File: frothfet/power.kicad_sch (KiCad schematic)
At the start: 46 parts, among them J2 Screw_Terminal_01x08, J3 Screw_Terminal_01x08, U26 TPS7A2033PDBVR, U27 XL1509-5.0, U28 MCP3425A0T-ECH, U29 MAX40200AUK

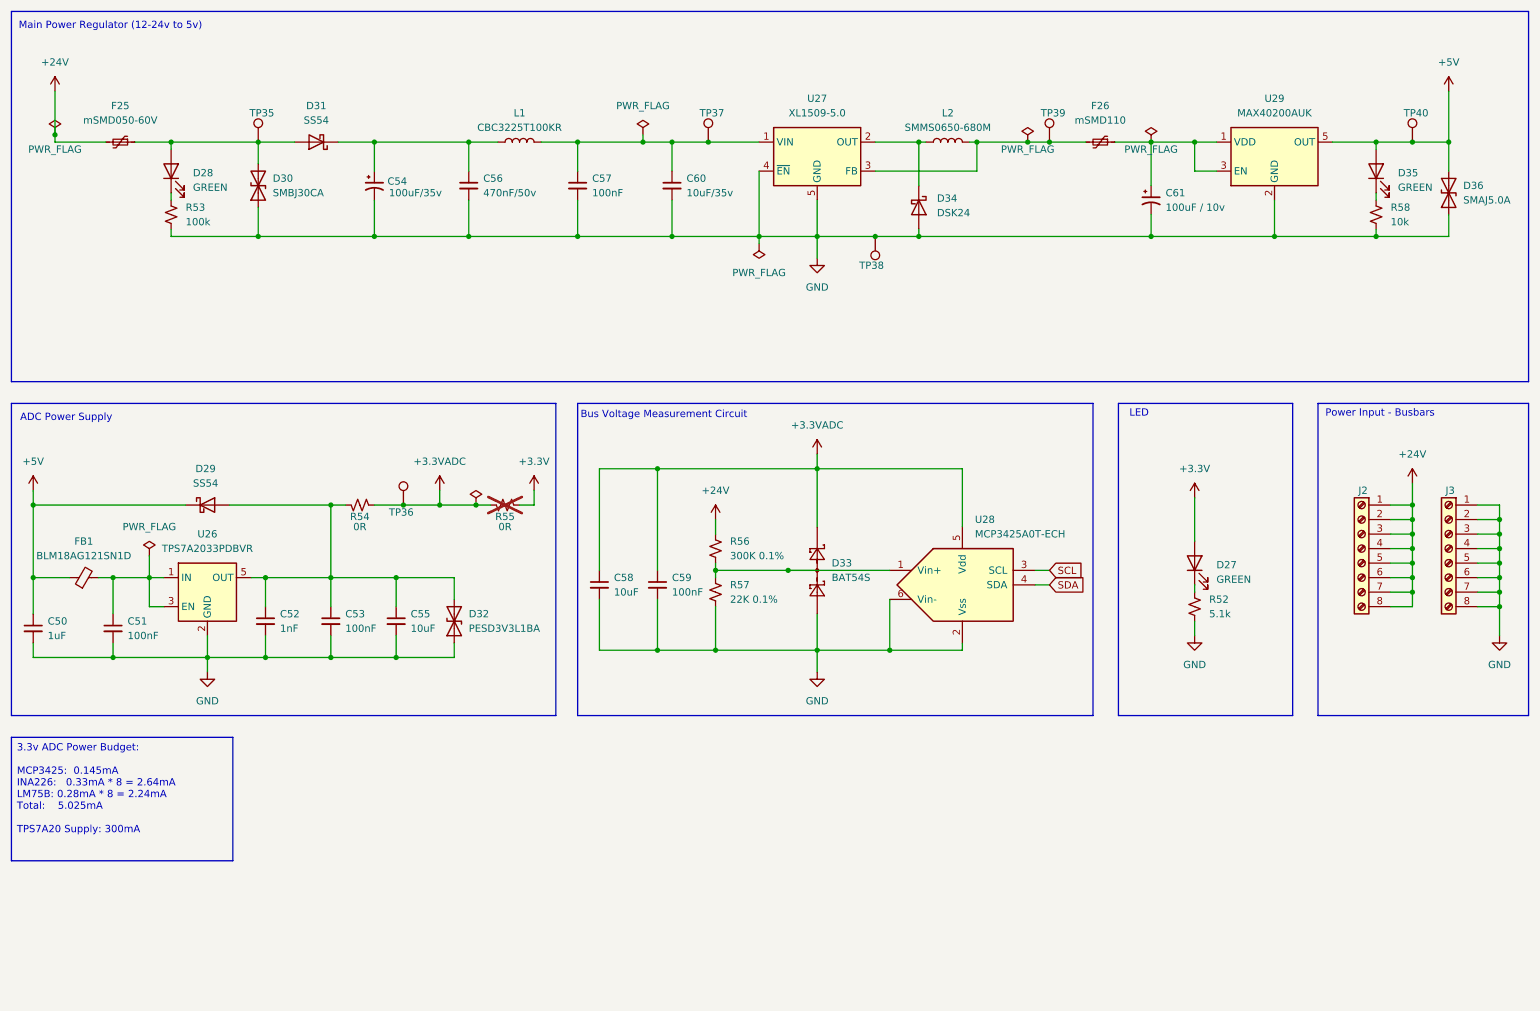
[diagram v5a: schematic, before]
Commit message: add esd protection to each channel output
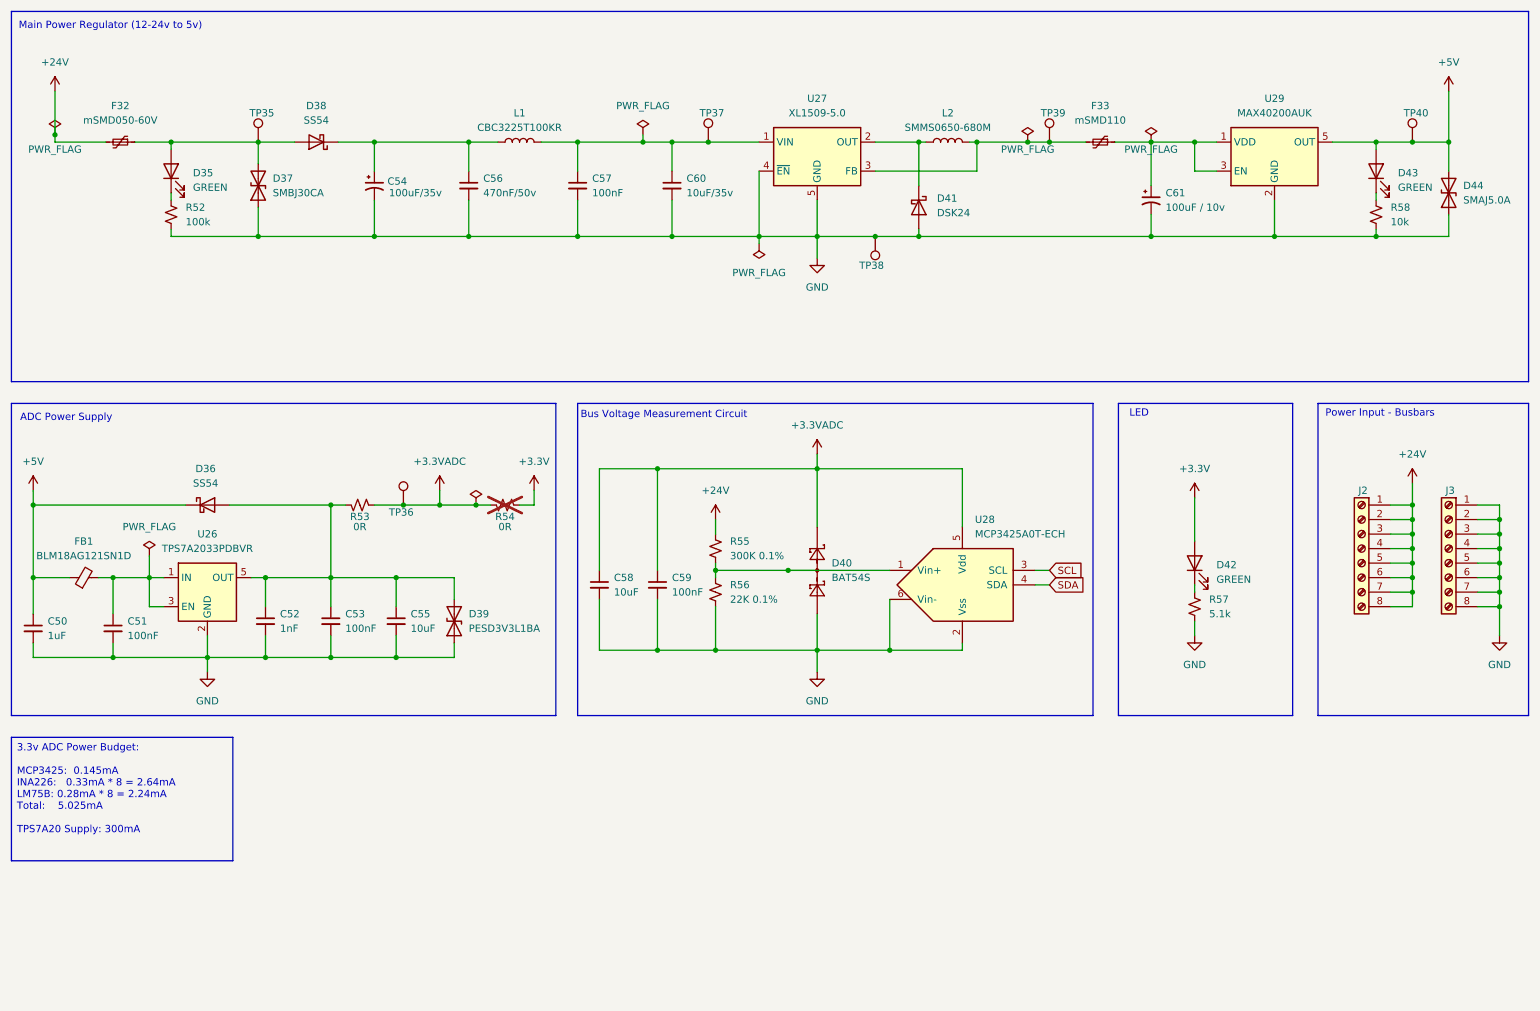
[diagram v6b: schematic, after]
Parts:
- renumbered D28 to D35, D29 to D36, D30 to D37, D31 to D38, D32 to D39, D33 to D40, D34 to D41, D27 to D42, D35 to D43, D36 to D44, F25 to F32, F26 to F33, R53 to R52, R54 to R53, R55 to R54, R56 to R55, R57 to R56, R52 to R57
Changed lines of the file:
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@@
 		(dnp no)
 		(fields_autoplaced yes)
-		(property "Reference" "D33"
+		(property "Reference" "D40"
 			(at 158.75 111.76 90)
 			(effects
@@
 			(project "8ch-mosfet"
 				(path "/c83c6236-96e9-46ad-9d7a-9e2efa4a7966/e112a34f-fd2f-43cb-bf5d-a7f5e57b6bef"
-					(reference "D33")
+					(reference "D40")
 					(unit 1)
 				)
@@
 		(dnp no)
 		(fields_autoplaced yes)
-		(property "Reference" "R53"
+		(property "Reference" "R52"
 			(at 45.72 49.5299 0)
 			(effects
@@
 			(project "frothfet"
 				(path "/c83c6236-96e9-46ad-9d7a-9e2efa4a7966/e112a34f-fd2f-43cb-bf5d-a7f5e57b6bef"
-					(reference "R53")
+					(reference "R52")
 					(unit 1)
 				)
@@
 		(dnp no)
 		(fields_autoplaced yes)
-		(property "Reference" "D34"
+		(property "Reference" "D41"
 			(at 177.165 47.9425 90)
 			(effects
@@
 			(project "8ch-mosfet"
 				(path "/c83c6236-96e9-46ad-9d7a-9e2efa4a7966/e112a34f-fd2f-43cb-bf5d-a7f5e57b6bef"
-					(reference "D34")
+					(reference "D41")
 					(unit 1)
 				)
@@
 		(dnp no)
 		(fields_autoplaced yes)
-		(property "Reference" "D28"
+		(property "Reference" "D35"
 			(at 46.99 43.4974 90)
 			(effects
@@
 			(project "frothfet"
 				(path "/c83c6236-96e9-46ad-9d7a-9e2efa4a7966/e112a34f-fd2f-43cb-bf5d-a7f5e57b6bef"
-					(reference "D28")
+					(reference "D35")
 					(unit 1)
 				)
@@
 		(dnp no)
 		(fields_autoplaced yes)
-		(property "Reference" "#PWR0137"
+		(property "Reference" "#PWR0135"
 			(at 106.68 102.87 0)
 			(effects
@@
 			(project "frothfet"
 				(path "/c83c6236-96e9-46ad-9d7a-9e2efa4a7966/e112a34f-fd2f-43cb-bf5d-a7f5e57b6bef"
-					(reference "#PWR0137")
+					(reference "#PWR0135")
 					(unit 1)
 				)
@@
 		(dnp no)
 		(fields_autoplaced yes)
-		(property "Reference" "#PWR0133"
+		(property "Reference" "#PWR0140"
 			(at 222.25 104.14 0)
 			(effects
@@
 			(project "frothfet"
 				(path "/c83c6236-96e9-46ad-9d7a-9e2efa4a7966/e112a34f-fd2f-43cb-bf5d-a7f5e57b6bef"
-					(reference "#PWR0133")
+					(reference "#PWR0140")
 					(unit 1)
 				)
@@
 		(dnp no)
 		(fields_autoplaced yes)
-		(property "Reference" "D27"
+		(property "Reference" "D42"
 			(at 226.06 112.0774 90)
 			(effects
@@
 			(project "frothfet"
 				(path "/c83c6236-96e9-46ad-9d7a-9e2efa4a7966/e112a34f-fd2f-43cb-bf5d-a7f5e57b6bef"
-					(reference "D27")
+					(reference "D42")
 					(unit 1)
 				)
@@
 		(dnp no)
 		(fields_autoplaced yes)
-		(property "Reference" "#PWR0141"
+		(property "Reference" "#PWR0139"
 			(at 156.21 137.16 0)
 			(effects
@@
 			(project "frothfet"
 				(path "/c83c6236-96e9-46ad-9d7a-9e2efa4a7966/e112a34f-fd2f-43cb-bf5d-a7f5e57b6bef"
-					(reference "#PWR0141")
+					(reference "#PWR0139")
 					(unit 1)
 				)
@@
 		(dnp no)
 		(fields_autoplaced yes)
-		(property "Reference" "#PWR0136"
+		(property "Reference" "#PWR0134"
 			(at 86.36 100.33 0)
 			(effects
@@
 			(project ""
 				(path "/c83c6236-96e9-46ad-9d7a-9e2efa4a7966/e112a34f-fd2f-43cb-bf5d-a7f5e57b6bef"
-					(reference "#PWR0136")
+					(reference "#PWR0134")
 					(unit 1)
 				)
@@
 		(on_board yes)
 		(dnp no)
-		(property "Reference" "D30"
+		(property "Reference" "D37"
 			(at 60.96 44.45 90)
 			(effects
@@
 			(project "8ch-mosfet"
 				(path "/c83c6236-96e9-46ad-9d7a-9e2efa4a7966/e112a34f-fd2f-43cb-bf5d-a7f5e57b6bef"
-					(reference "D30")
+					(reference "D37")
 					(unit 1)
 				)
@@
 		(on_board yes)
 		(dnp no)
-		(property "Reference" "D29"
+		(property "Reference" "D36"
 			(at 49.2125 95.25 0)
 			(effects
@@
 			(project "frothfet"
 				(path "/c83c6236-96e9-46ad-9d7a-9e2efa4a7966/e112a34f-fd2f-43cb-bf5d-a7f5e57b6bef"
-					(reference "D29")
+					(reference "D36")
 					(unit 1)
 				)
@@
 		(dnp no)
 		(fields_autoplaced yes)
-		(property "Reference" "R56"
+		(property "Reference" "R55"
 			(at 140.97 107.95 0)
 			(effects
@@
 			(project "8ch-mosfet"
 				(path "/c83c6236-96e9-46ad-9d7a-9e2efa4a7966/e112a34f-fd2f-43cb-bf5d-a7f5e57b6bef"
-					(reference "R56")
+					(reference "R55")
 					(unit 1)
 				)
@@
 		(dnp no)
 		(fields_autoplaced yes)
-		(property "Reference" "#PWR0134"
+		(property "Reference" "#PWR0141"
 			(at 222.25 130.81 0)
 			(effects
@@
 			(project "frothfet"
 				(path "/c83c6236-96e9-46ad-9d7a-9e2efa4a7966/e112a34f-fd2f-43cb-bf5d-a7f5e57b6bef"
-					(reference "#PWR0134")
+					(reference "#PWR0141")
 					(unit 1)
 				)
@@
 		(dnp no)
 		(fields_autoplaced yes)
-		(property "Reference" "#PWR0138"
+		(property "Reference" "#PWR0136"
 			(at 138.43 107.95 0)
 			(effects
@@
 			(project "8ch-mosfet"
 				(path "/c83c6236-96e9-46ad-9d7a-9e2efa4a7966/e112a34f-fd2f-43cb-bf5d-a7f5e57b6bef"
-					(reference "#PWR0138")
+					(reference "#PWR0136")
 					(unit 1)
 				)
@@
 		(dnp no)
 		(fields_autoplaced yes)
-		(property "Reference" "F26"
+		(property "Reference" "F33"
 			(at 205.74 31.75 90)
 			(effects
@@
 			(project "8ch-mosfet"
 				(path "/c83c6236-96e9-46ad-9d7a-9e2efa4a7966/e112a34f-fd2f-43cb-bf5d-a7f5e57b6bef"
-					(reference "F26")
+					(reference "F33")
 					(unit 1)
 				)
@@
 		(dnp no)
 		(fields_autoplaced yes)
-		(property "Reference" "D35"
+		(property "Reference" "D43"
 			(at 257.81 43.4974 90)
 			(effects
@@
 			(project "frothfet"
 				(path "/c83c6236-96e9-46ad-9d7a-9e2efa4a7966/e112a34f-fd2f-43cb-bf5d-a7f5e57b6bef"
-					(reference "D35")
+					(reference "D43")
 					(unit 1)
 				)
@@
 		(dnp no)
 		(fields_autoplaced yes)
-		(property "Reference" "F25"
+		(property "Reference" "F32"
 			(at 34.29 31.75 90)
 			(effects
@@
 			(project "8ch-mosfet"
 				(path "/c83c6236-96e9-46ad-9d7a-9e2efa4a7966/e112a34f-fd2f-43cb-bf5d-a7f5e57b6bef"
-					(reference "F25")
+					(reference "F32")
 					(unit 1)
 				)
@@
 		(dnp no)
 		(fields_autoplaced yes)
-		(property "Reference" "#PWR0139"
+		(property "Reference" "#PWR0137"
 			(at 156.21 64.77 0)
 			(effects
@@
 			(project "8ch-mosfet"
 				(path "/c83c6236-96e9-46ad-9d7a-9e2efa4a7966/e112a34f-fd2f-43cb-bf5d-a7f5e57b6bef"
-					(reference "#PWR0139")
+					(reference "#PWR0137")
 					(unit 1)
 				)
@@
 		(on_board yes)
 		(dnp no)
-		(property "Reference" "R54"
+		(property "Reference" "R53"
 			(at 76.2 103.632 90)
 			(effects
@@
 			(project "frothfet"
 				(path "/c83c6236-96e9-46ad-9d7a-9e2efa4a7966/e112a34f-fd2f-43cb-bf5d-a7f5e57b6bef"
-					(reference "R54")
+					(reference "R53")
 					(unit 1)
 				)
@@
 		(on_board yes)
 		(dnp no)
-		(property "Reference" "D36"
+		(property "Reference" "D44"
 			(at 269.24 45.72 90)
 			(effects
@@
 			(project "frothfet"
 				(path "/c83c6236-96e9-46ad-9d7a-9e2efa4a7966/e112a34f-fd2f-43cb-bf5d-a7f5e57b6bef"
-					(reference "D36")
+					(reference "D44")
 					(unit 1)
 				)
@@
 		(dnp no)
 		(fields_autoplaced yes)
-		(property "Reference" "#PWR0135"
+		(property "Reference" "#PWR0133"
 			(at 49.53 137.16 0)
 			(effects
@@
 			(project ""
 				(path "/c83c6236-96e9-46ad-9d7a-9e2efa4a7966/e112a34f-fd2f-43cb-bf5d-a7f5e57b6bef"
-					(reference "#PWR0135")
+					(reference "#PWR0133")
 					(unit 1)
 				)
@@
 		(on_board yes)
 		(dnp yes)
-		(property "Reference" "R55"
+		(property "Reference" "R54"
 			(at 101.6 103.632 90)
 			(effects
@@
 			(project "frothfet"
 				(path "/c83c6236-96e9-46ad-9d7a-9e2efa4a7966/e112a34f-fd2f-43cb-bf5d-a7f5e57b6bef"
-					(reference "R55")
+					(reference "R54")
 					(unit 1)
 				)
@@
 		(dnp no)
 		(fields_autoplaced yes)
-		(property "Reference" "R57"
+		(property "Reference" "R56"
 			(at 140.97 115.57 0)
 			(effects
@@
 			(project "8ch-mosfet"
 				(path "/c83c6236-96e9-46ad-9d7a-9e2efa4a7966/e112a34f-fd2f-43cb-bf5d-a7f5e57b6bef"
-					(reference "R57")
+					(reference "R56")
 					(unit 1)
 				)
@@
 		(dnp no)
 		(fields_autoplaced yes)
-		(property "Reference" "D31"
+		(property "Reference" "D38"
 			(at 68.58 31.75 0)
 			(effects
@@
 			(project "8ch-mosfet"
 				(path "/c83c6236-96e9-46ad-9d7a-9e2efa4a7966/e112a34f-fd2f-43cb-bf5d-a7f5e57b6bef"
-					(reference "D31")
+					(reference "D38")
 					(unit 1)
 				)
@@
 		(on_board yes)
 		(dnp no)
-		(property "Reference" "D32"
+		(property "Reference" "D39"
 			(at 95.25 120.65 90)
 			(effects
@@
 			(project "frothfet"
 				(path "/c83c6236-96e9-46ad-9d7a-9e2efa4a7966/e112a34f-fd2f-43cb-bf5d-a7f5e57b6bef"
-					(reference "D32")
+					(reference "D39")
 					(unit 1)
 				)
@@
 		(dnp no)
 		(fields_autoplaced yes)
-		(property "Reference" "R52"
+		(property "Reference" "R57"
 			(at 224.79 118.1099 0)
 			(effects
@@
 			(project "frothfet"
 				(path "/c83c6236-96e9-46ad-9d7a-9e2efa4a7966/e112a34f-fd2f-43cb-bf5d-a7f5e57b6bef"
-					(reference "R52")
+					(reference "R57")
 					(unit 1)
 				)
@@
 		(dnp no)
 		(fields_autoplaced yes)
-		(property "Reference" "#PWR0140"
+		(property "Reference" "#PWR0138"
 			(at 160.02 93.98 0)
 			(effects
@@
 			(project "frothfet"
 				(path "/c83c6236-96e9-46ad-9d7a-9e2efa4a7966/e112a34f-fd2f-43cb-bf5d-a7f5e57b6bef"
-					(reference "#PWR0140")
+					(reference "#PWR0138")
 					(unit 1)
 				)

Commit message: pulled in latest version of esp32 schematic
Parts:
- removed D42: GREEN, LED_SMD:LED_0603_1608Metric, symbol Device:LED
- removed R57: 5.1k, Resistor_SMD:R_0603_1608Metric, symbol Device:R_Small_US
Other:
- note removed: "LED"

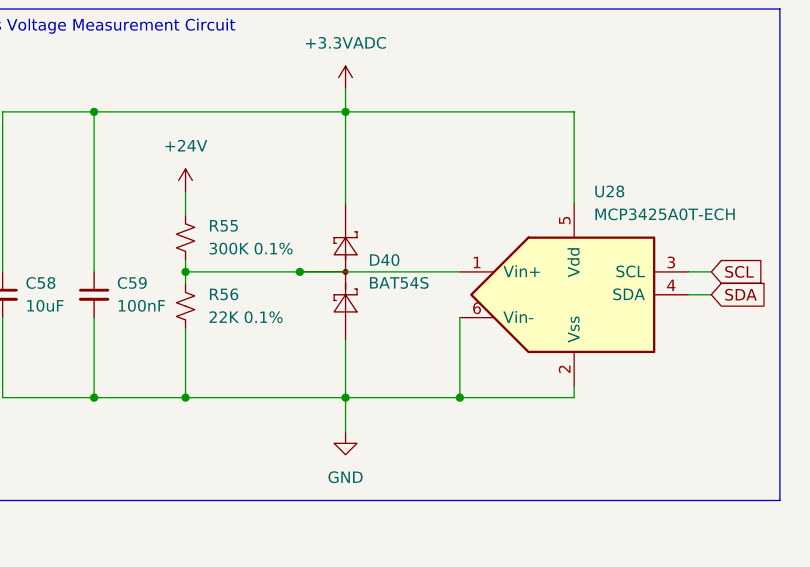
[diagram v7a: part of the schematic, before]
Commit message: switched to bav199 on bus voltage
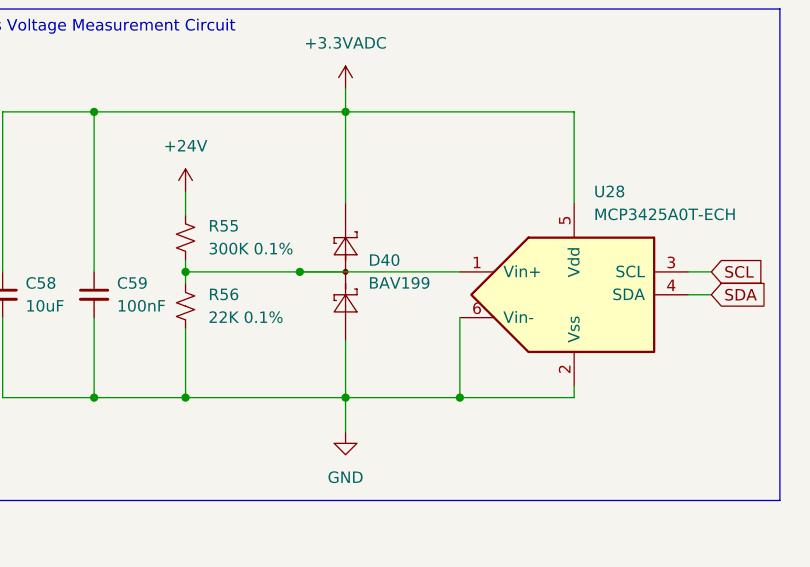
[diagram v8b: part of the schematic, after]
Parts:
- D40: value BAT54S -> BAV199; LCSC C727126 -> C40919
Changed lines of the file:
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@@
 			)
 		)
-		(property "Value" "BAT54S"
+		(property "Value" "BAV199"
 			(at 158.75 114.3 90)
 			(effects
@@
 			)
 		)
-		(property "Datasheet" "https://www.diodes.com/assets/Datasheets/ds11005.pdf"
+		(property "Datasheet" "https://www.lcsc.com/datasheet/C40919.pdf"
 			(at 156.21 116.078 0)
 			(effects
@@
 			)
 		)
-		(property "LCSC" "C727126"
+		(property "LCSC" "C40919"
 			(at 156.21 113.03 90)
 			(effects
